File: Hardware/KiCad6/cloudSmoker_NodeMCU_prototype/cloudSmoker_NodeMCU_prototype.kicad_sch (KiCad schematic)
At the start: 22 parts, among them J1 Conn_01x05_Male, J2 Conn_01x04_Male, J3 Conn_01x03_Male, J4 Conn_01x03_Male, U1 NodeMCU1.0(ESP-12E), U2 ADS1015IDGS

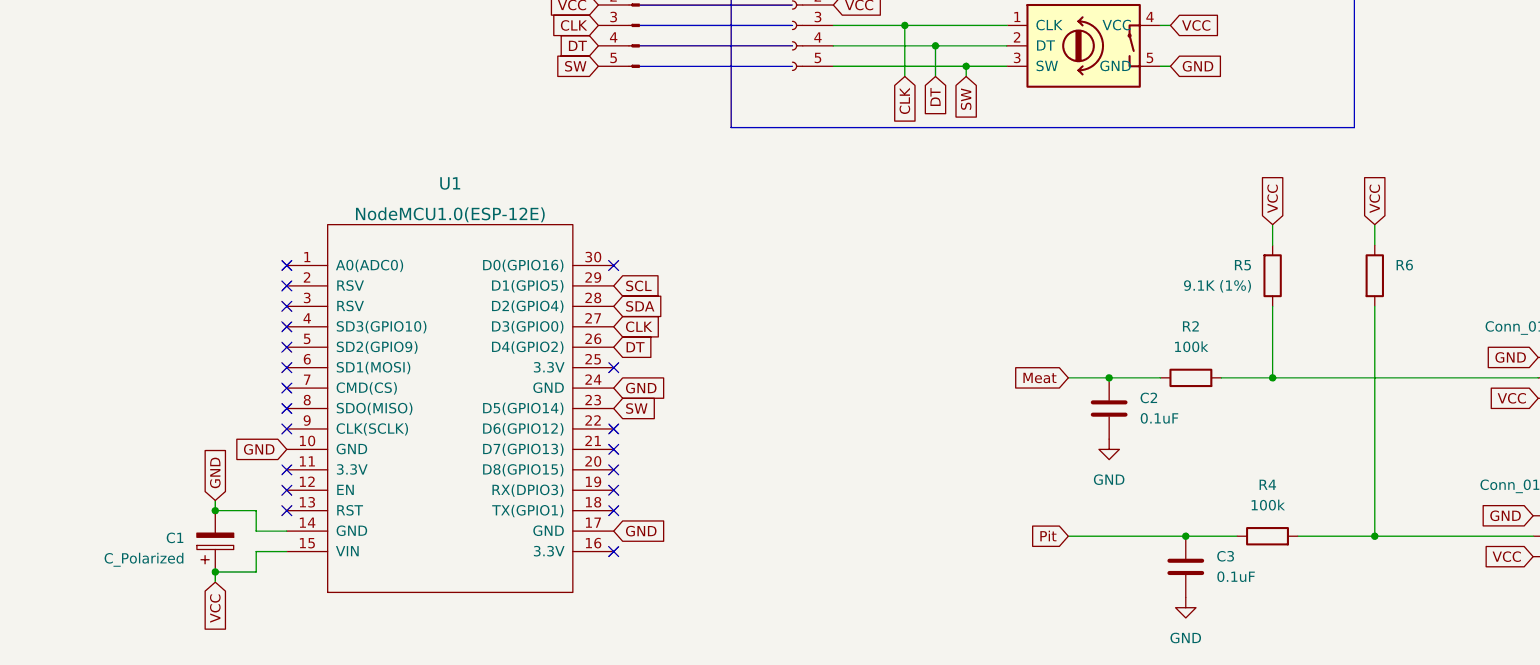
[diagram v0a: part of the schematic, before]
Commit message: update schematic
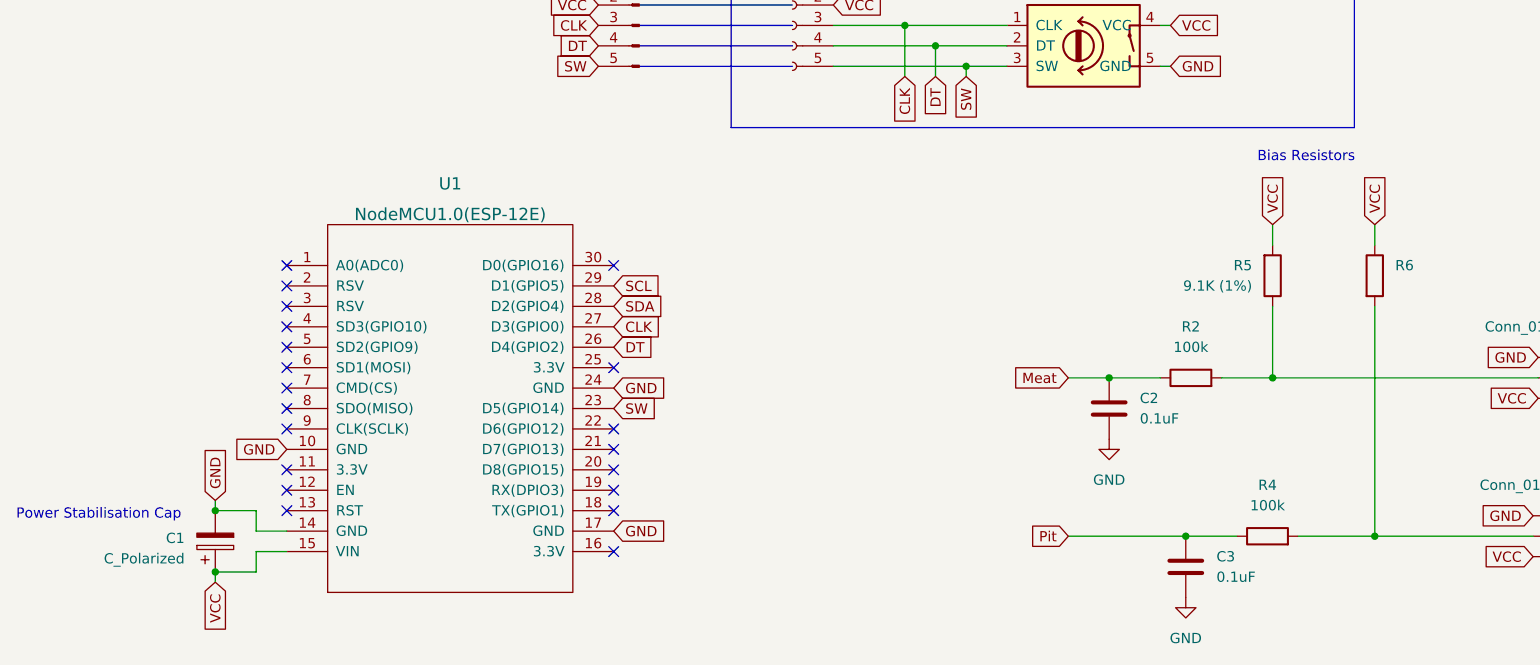
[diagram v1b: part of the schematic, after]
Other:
- note added: "Bias Resistors"
- note added: "Power Stabilisation Cap"
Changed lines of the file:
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@@
+    (effects (font (size 1.27 1.27)) (justify left bottom))
+  )
+  (text "Power Stabilisation Cap" (at 13.335 147.955 0)
     (effects (font (size 1.27 1.27)) (justify left bottom))
   )
@@
     (effects (font (size 1.27 1.27)) (justify left bottom))
   )
+  (text "Bias Resistors" (at 167.64 103.505 0)
+    (effects (font (size 1.27 1.27)) (justify left bottom))
+  )
